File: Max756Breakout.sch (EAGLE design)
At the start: 10 parts

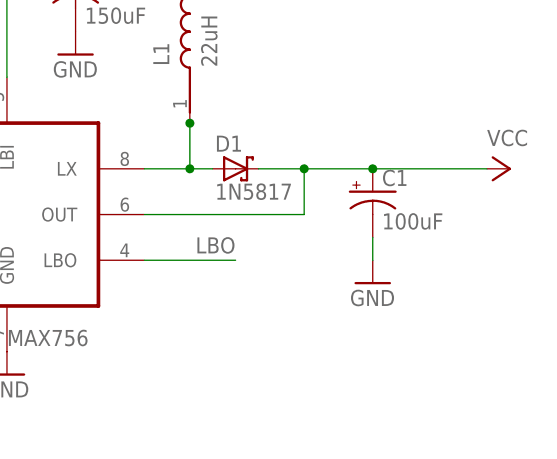
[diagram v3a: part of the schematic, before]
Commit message: Added LED for v2
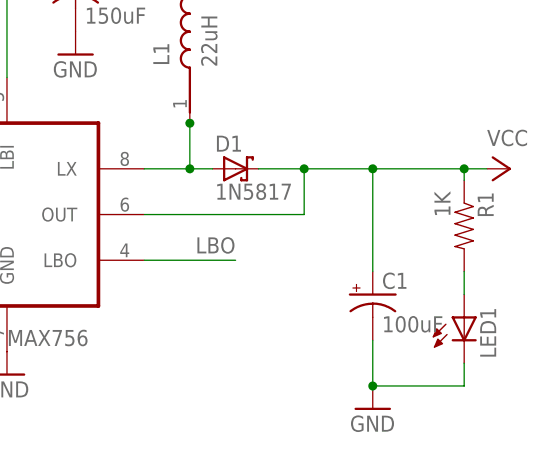
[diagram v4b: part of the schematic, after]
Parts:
- added LED1: (no value), Dek:LED3MM
- added R1: 1K, Dek:RESISTORAXIAL-0.2
- C1, C2: device SparkFun-Capacitors:CAP_POLPTH1 -> SparkFun-Capacitors:CAP_POLPTH2
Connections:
- new net N$2: LED1.A, R1.2
- net GND: now also LED1.C
- net VCC: now also R1.1
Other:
- moved on the sheet: C1
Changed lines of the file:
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@@
 <setting verticaltext="up"/>
 </settings>
-<grid distance="0.1" unitdist="inch" unit="inch" style="lines" multiple="1" display="no" altdistance="0.01" altunitdist="inch" altunit="inch"/>
+<grid distance="0.05" unitdist="inch" unit="inch" style="lines" multiple="1" display="yes" altdistance="0.005" altunitdist="inch" altunit="inch"/>
 <layers>
-<layer number="1" name="Top" color="4" fill="1" visible="no" active="no"/>
-<layer number="16" name="Bottom" color="1" fill="1" visible="no" active="no"/>
-<layer number="17" name="Pads" color="2" fill="1" visible="no" active="no"/>
-<layer number="18" name="Vias" color="2" fill="1" visible="no" active="no"/>
-<layer number="19" name="Unrouted" color="6" fill="1" visible="no" active="no"/>
-<layer number="20" name="Dimension" color="15" fill="1" visible="no" active="no"/>
-<layer number="21" name="tPlace" color="16" fill="1" visible="no" active="no"/>
-<layer number="22" name="bPlace" color="14" fill="1" visible="no" active="no"/>
-<layer number="23" name="tOrigins" color="15" fill="1" visible="no" active="no"/>
-<layer number="24" name="bOrigins" color="15" fill="1" visible="no" active="no"/>
-<layer number="25" name="tNames" color="16" fill="1" visible="no" active="no"/>
-<layer number="26" name="bNames" color="7" fill="1" visible="no" active="no"/>
-<layer number="27" name="tValues" color="7" fill="1" visible="no" active="no"/>
-<layer number="28" name="bValues" color="7" fill="1" visible="no" active="no"/>
+<layer number="1" name="Top" color="4" fill="1" visible="yes" active="no"/>
+<layer number="16" name="Bottom" color="1" fill="1" visible="yes" active="no"/>
+<layer number="17" name="Pads" color="2" fill="1" visible="yes" active="no"/>
+<layer number="18" name="Vias" color="2" fill="1" visible="yes" active="no"/>
+<layer number="19" name="Unrouted" color="6" fill="1" visible="yes" active="no"/>
+<layer number="20" name="Dimension" color="15" fill="1" visible="yes" active="no"/>
+<layer number="21" name="tPlace" color="16" fill="1" visible="yes" active="no"/>
+<layer number="22" name="bPlace" color="14" fill="1" visible="yes" active="no"/>
+<layer number="23" name="tOrigins" color="15" fill="1" visible="yes" active="no"/>
+<layer number="24" name="bOrigins" color="15" fill="1" visible="yes" active="no"/>
+<layer number="25" name="tNames" color="16" fill="1" visible="yes" active="no"/>
+<layer number="26" name="bNames" color="7" fill="1" visible="yes" active="no"/>
+<layer number="27" name="tValues" color="7" fill="1" visible="yes" active="no"/>
+<layer number="28" name="bValues" color="7" fill="1" visible="yes" active="no"/>
 <layer number="29" name="tStop" color="7" fill="3" visible="no" active="no"/>
 <layer number="30" name="bStop" color="7" fill="6" visible="no" active="no"/>
@@
 <layer number="35" name="tGlue" color="7" fill="4" visible="no" active="no"/>
 <layer number="36" name="bGlue" color="7" fill="5" visible="no" active="no"/>
-<layer number="37" name="tTest" color="7" fill="1" visible="no" active="no"/>
-<layer number="38" name="bTest" color="7" fill="1" visible="no" active="no"/>
+<layer number="37" name="tTest" color="7" fill="1" visible="yes" active="no"/>
+<layer number="38" name="bTest" color="7" fill="1" visible="yes" active="no"/>
 <layer number="39" name="tKeepout" color="4" fill="11" visible="no" active="no"/>
 <layer number="40" name="bKeepout" color="1" fill="11" visible="no" active="no"/>
@@
 <layer number="44" name="Drills" color="7" fill="1" visible="no" active="no"/>
 <layer number="45" name="Holes" color="7" fill="1" visible="no" active="no"/>
-<layer number="46" name="Milling" color="3" fill="1" visible="no" active="no"/>
-<layer number="47" name="Measures" color="7" fill="1" visible="no" active="no"/>
-<layer number="48" name="Document" color="7" fill="1" visible="no" active="no"/>
-<layer number="49" name="Reference" color="7" fill="1" visible="no" active="no"/>
-<layer number="50" name="dxf" color="7" fill="1" visible="no" active="no"/>
-<layer number="51" name="tDocu" color="6" fill="1" visible="no" active="no"/>
-<layer number="52" name="bDocu" color="7" fill="1" visible="no" active="no"/>
-<layer number="53" name="tGND_GNDA" color="7" fill="9" visible="no" active="no"/>
-<layer number="54" name="bGND_GNDA" color="1" fill="9" visible="no" active="no"/>
-<layer number="56" name="wert" color="7" fill="1" visible="no" active="no"/>
+<layer number="46" name="Milling" color="3" fill="1" visible="yes" active="no"/>
+<layer number="47" name="Measures" color="7" fill="1" visible="yes" active="no"/>
+<layer number="48" name="Document" color="7" fill="1" visible="yes" active="no"/>
+<layer number="49" name="Reference" color="7" fill="1" visible="yes" active="no"/>
+<layer number="50" name="dxf" color="7" fill="1" visible="yes" active="no"/>
+<layer number="51" name="tDocu" color="6" fill="1" visible="yes" active="no"/>
+<layer number="52" name="bDocu" color="7" fill="1" visible="yes" active="no"/>
+<layer number="53" name="tGND_GNDA" color="7" fill="9" visible="yes" active="no"/>
+<layer number="54" name="bGND_GNDA" color="1" fill="9" visible="yes" active="no"/>
+<layer number="56" name="wert" color="7" fill="1" visible="yes" active="no"/>
 <layer number="91" name="Nets" color="2" fill="1" visible="yes" active="yes"/>
 <layer number="92" name="Busses" color="1" fill="1" visible="yes" active="yes"/>
@@
 <parts>
 <part name="MAX756" library="adafruit" deviceset="MAX756" device="CPA"/>
-<part name="C1" library="SparkFun-Capacitors" deviceset="CAP_POL" device="PTH1" value="100uF"/>
-<part name="C2" library="SparkFun-Capacitors" deviceset="CAP_POL" device="PTH1" value="150uF"/>
+<part name="C1" library="SparkFun-Capacitors" deviceset="CAP_POL" device="PTH2" value="100uF"/>
+<part name="C2" library="SparkFun-Capacitors" deviceset="CAP_POL" device="PTH2" value="150uF"/>
 <part name="GND1" library="supply1" deviceset="GND" device=""/>
 <part name="GND2" library="supply1" deviceset="GND" device=""/>
@@
 <part name="GND7" library="supply1" deviceset="GND" device=""/>
 <part name="OUT" library="SparkFun-Connectors" deviceset="M02" device="LOCK"/>
+<part name="LED1" library="Dek" deviceset="LED" device="3MM"/>
+<part name="R1" library="Dek" deviceset="RESISTOR" device="AXIAL-0.2" value="1K"/>
 </parts>
 <sheets>
@@
 <instances>
 <instance part="MAX756" gate="G$1" x="25.4" y="46.99"/>
-<instance part="C1" gate="G$1" x="68.58" y="49.53"/>
+<instance part="C1" gate="G$1" x="68.58" y="38.1"/>
 <instance part="C2" gate="G$1" x="35.56" y="72.39"/>
-<instance part="GND1" gate="1" x="68.58" y="39.37"/>
+<instance part="GND1" gate="1" x="68.58" y="25.4"/>
 <instance part="GND2" gate="1" x="35.56" y="64.77"/>
 <instance part="GND3" gate="1" x="27.94" y="29.21"/>
@@
 <instance part="GND7" gate="1" x="76.2" y="104.14" rot="R180"/>
 <instance part="OUT" gate="G$1" x="64.77" y="99.06"/>
+<instance part="LED1" gate="G$1" x="78.74" y="35.56"/>
+<instance part="R1" gate="G$1" x="78.74" y="45.72" rot="R270"/>
 </instances>
 <busses>
@@
 <pinref part="C1" gate="G$1" pin="-"/>
 <pinref part="GND1" gate="1" pin="GND"/>
-<wire x1="68.58" y1="41.91" x2="68.58" y2="44.45" width="0.1524" layer="91"/>
+<wire x1="68.58" y1="27.94" x2="68.58" y2="33.02" width="0.1524" layer="91"/>
+<pinref part="LED1" gate="G$1" pin="C"/>
+<wire x1="78.74" y1="30.48" x2="78.74" y2="27.94" width="0.1524" layer="91"/>
+<wire x1="78.74" y1="27.94" x2="68.58" y2="27.94" width="0.1524" layer="91"/>
+<junction x="68.58" y="27.94"/>
 </segment>
 <segment>
@@
 <net name="VCC" class="1">
 <segment>
-<pinref part="C1" gate="G$1" pin="+"/>
+<pinref part="P+1" gate="VCC" pin="VCC"/>
+<wire x1="78.74" y1="52.07" x2="81.28" y2="52.07" width="0.1524" layer="91"/>
+<pinref part="R1" gate="G$1" pin="1"/>
+<wire x1="78.74" y1="50.8" x2="78.74" y2="52.07" width="0.1524" layer="91"/>
 <wire x1="55.88" y1="52.07" x2="60.96" y2="52.07" width="0.1524" layer="91"/>
 <pinref part="MAX756" gate="G$1" pin="OUT"/>
-<wire x1="60.96" y1="52.07" x2="68.58" y2="52.07" width="0.1524" layer="91"/>
 <wire x1="43.18" y1="46.99" x2="60.96" y2="46.99" width="0.1524" layer="91"/>
 <wire x1="60.96" y1="46.99" x2="60.96" y2="52.07" width="0.1524" layer="91"/>
+<pinref part="D1" gate="G$1" pin="C"/>
+<wire x1="78.74" y1="52.07" x2="68.58" y2="52.07" width="0.1524" layer="91"/>
+<junction x="78.74" y="52.07"/>
 <junction x="60.96" y="52.07"/>
-<wire x1="68.58" y1="52.07" x2="81.28" y2="52.07" width="0.1524" layer="91"/>
+<pinref part="C1" gate="G$1" pin="+"/>
+<wire x1="68.58" y1="52.07" x2="60.96" y2="52.07" width="0.1524" layer="91"/>
+<wire x1="68.58" y1="52.07" x2="68.58" y2="40.64" width="0.1524" layer="91"/>
 <junction x="68.58" y="52.07"/>
-<pinref part="P+1" gate="VCC" pin="VCC"/>
-<pinref part="D1" gate="G$1" pin="C"/>
 </segment>
 <segment>
@@
 </segment>
 </net>
+<net name="N$2" class="0">
+<segment>
+<pinref part="LED1" gate="G$1" pin="A"/>
+<pinref part="R1" gate="G$1" pin="2"/>
+<wire x1="78.74" y1="40.64" x2="78.74" y2="38.1" width="0.1524" layer="91"/>
+</segment>
+</net>

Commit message: Exported PDF schematic
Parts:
- added FRAME1: FRAME-LETTER, SparkFun-Aesthetics:FRAME-LETTER
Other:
- moved on the sheet: 3/5, BRIDGE, C1, C2, C3, D1, L1, LED1, MAX756, OUT, PWR, R1
